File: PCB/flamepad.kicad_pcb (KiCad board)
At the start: 2 copper layers, 77.7 x 96.9 mm, 26 parts, among them J1 Conn_01x04_Pin, SW1 RotaryEncoder_Switch, SW10 SW_Push, SW11 SW_Push, SW12 SW_Push, SW2 SW_Push, SW3 SW_Push, SW4 SW_Push, SW5 SW_Push, SW6 SW_Push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

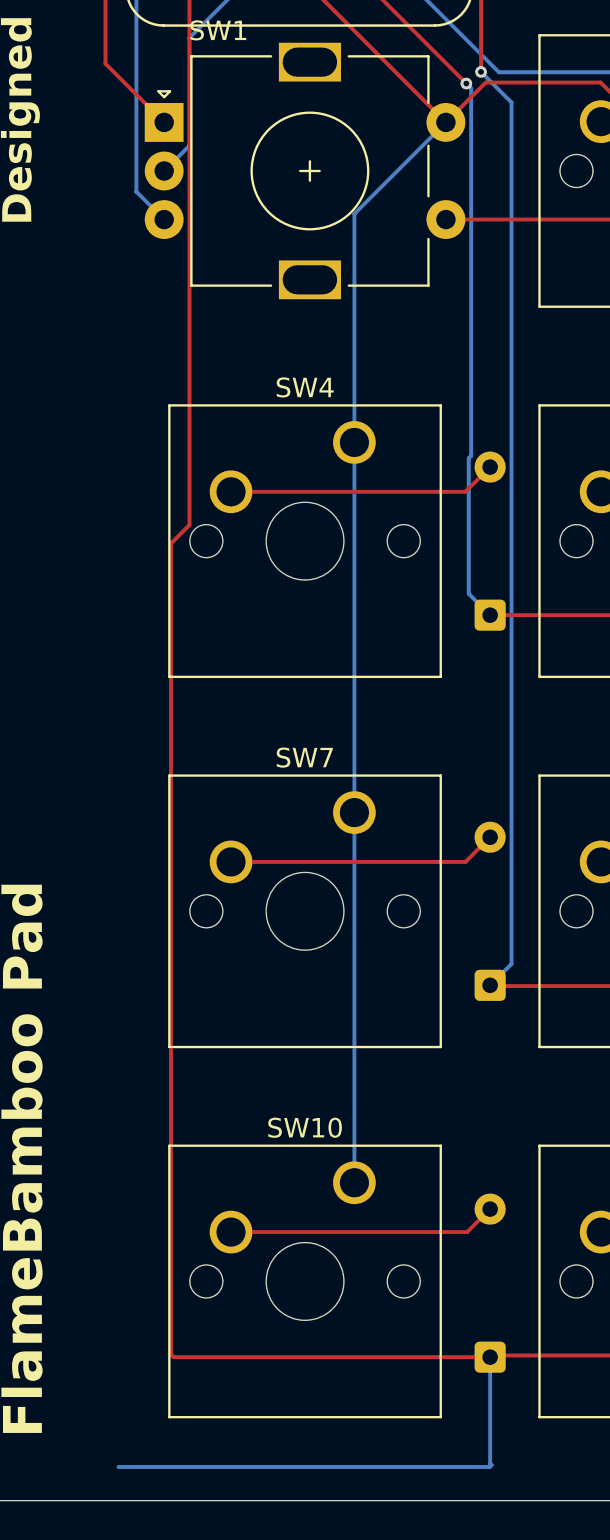
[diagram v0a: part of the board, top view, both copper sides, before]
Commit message: prodfil Gerber update due to mislook mistake in DRC check.
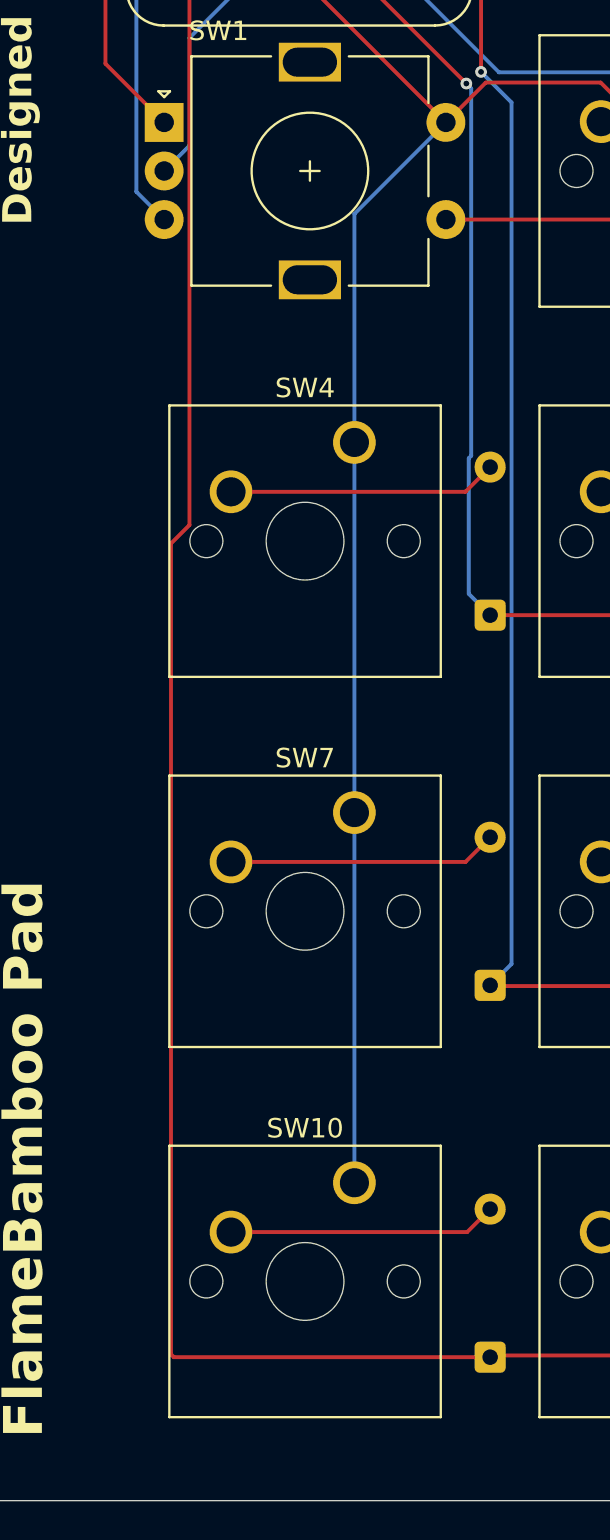
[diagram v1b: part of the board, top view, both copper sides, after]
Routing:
- net Row 3: track 159.5 -> 134.6 mm
- net SW1 A: vias 2 -> 0
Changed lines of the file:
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@@
 			(outputformat 1)
 			(mirror no)
-			(drillshape 1)
+			(drillshape 0)
 			(scaleselection 1)
-			(outputdirectory "")
+			(outputdirectory "../production/")
 		)
 	)
@@
 		(property ki_fp_filters "RotaryEncoder*Switch*")
 		(sheetname "/")
-		(sheetfile "test.kicad_sch")
+		(sheetfile "flamepad.kicad_sch")
 		(attr through_hole)
 		(fp_line
@@
 		)
 		(sheetname "/")
-		(sheetfile "test.kicad_sch")
+		(sheetfile "flamepad.kicad_sch")
 		(attr through_hole)
 		(fp_line
@@
 		)
 		(sheetname "/")
-		(sheetfile "test.kicad_sch")
+		(sheetfile "flamepad.kicad_sch")
 		(attr through_hole)
 		(fp_line
@@
 		(property ki_fp_filters "Connector*:*_1x??_*")
 		(sheetname "/")
-		(sheetfile "test.kicad_sch")
+		(sheetfile "flamepad.kicad_sch")
 		(attr through_hole)
 		(fp_line
@@
 		)
 		(sheetname "/")
-		(sheetfile "test.kicad_sch")
+		(sheetfile "flamepad.kicad_sch")
 		(attr through_hole)
 		(fp_line
@@
 		)
 		(sheetname "/")
-		(sheetfile "test.kicad_sch")
+		(sheetfile "flamepad.kicad_sch")
 		(attr through_hole)
 		(fp_line
@@
 		)
 		(sheetname "/")
-		(sheetfile "test.kicad_sch")
+		(sheetfile "flamepad.kicad_sch")
 		(attr through_hole)
 		(fp_line
@@
 		)
 		(sheetname "/")
-		(sheetfile "test.kicad_sch")
+		(sheetfile "flamepad.kicad_sch")
 		(attr through_hole)
 		(fp_line
@@
 		)
 		(sheetname "/")
-		(sheetfile "test.kicad_sch")
+		(sheetfile "flamepad.kicad_sch")
 		(attr through_hole)
 		(fp_line
@@
 		)
 		(sheetname "/")
-		(sheetfile "test.kicad_sch")
+		(sheetfile "flamepad.kicad_sch")
 		(attr through_hole)
 		(fp_line
@@
 		)
 		(sheetname "/")
-		(sheetfile "test.kicad_sch")
+		(sheetfile "flamepad.kicad_sch")
 		(attr through_hole)
 		(fp_line
@@
 		)
 		(sheetname "/")
-		(sheetfile "test.kicad_sch")
+		(sheetfile "flamepad.kicad_sch")
 		(attr smd)
 		(fp_line
@@
 		)
 		(sheetname "/")
-		(sheetfile "test.kicad_sch")
+		(sheetfile "flamepad.kicad_sch")
 		(attr through_hole)
 		(fp_line
@@
 		)
 		(sheetname "/")
-		(sheetfile "test.kicad_sch")
+		(sheetfile "flamepad.kicad_sch")
 		(attr through_hole)
 		(fp_line
@@
 		(property ki_fp_filters "D*DO?35*")
 		(sheetname "/")
-		(sheetfile "test.kicad_sch")
+		(sheetfile "flamepad.kicad_sch")
 		(attr through_hole)
 		(fp_line
@@
 		(property ki_fp_filters "D*DO?35*")
 		(sheetname "/")
-		(sheetfile "test.kicad_sch")
+		(sheetfile "flamepad.kicad_sch")
 		(attr through_hole)
 		(fp_line
@@
 		(property ki_fp_filters "D*DO?35*")
 		(sheetname "/")
-		(sheetfile "test.kicad_sch")
+		(sheetfile "flamepad.kicad_sch")
 		(attr through_hole)
 		(fp_line
@@
 		(property ki_fp_filters "D*DO?35*")
 		(sheetname "/")
-		(sheetfile "test.kicad_sch")
+		(sheetfile "flamepad.kicad_sch")
 		(attr through_hole)
 		(fp_line
@@
 		(property ki_fp_filters "D*DO?35*")
 		(sheetname "/")
-		(sheetfile "test.kicad_sch")
+		(sheetfile "flamepad.kicad_sch")
 		(attr through_hole)
 		(fp_line
@@
 		(property ki_fp_filters "D*DO?35*")
 		(sheetname "/")
-		(sheetfile "test.kicad_sch")
+		(sheetfile "flamepad.kicad_sch")
 		(attr through_hole)
 		(fp_line
@@
 		(property ki_fp_filters "D*DO?35*")
 		(sheetname "/")
-		(sheetfile "test.kicad_sch")
+		(sheetfile "flamepad.kicad_sch")
 		(attr through_hole)
 		(fp_line
@@
 		(property ki_fp_filters "D*DO?35*")
 		(sheetname "/")
-		(sheetfile "test.kicad_sch")
+		(sheetfile "flamepad.kicad_sch")
 		(attr through_hole)
 		(fp_line
@@
 		(property ki_fp_filters "D*DO?35*")
 		(sheetname "/")
-		(sheetfile "test.kicad_sch")
+		(sheetfile "flamepad.kicad_sch")
 		(attr through_hole)
 		(fp_line
@@
 		(property ki_fp_filters "D*DO?35*")
 		(sheetname "/")
-		(sheetfile "test.kicad_sch")
+		(sheetfile "flamepad.kicad_sch")
 		(attr through_hole)
 		(fp_line
@@
 		(property ki_fp_filters "D*DO?35*")
 		(sheetname "/")
-		(sheetfile "test.kicad_sch")
+		(sheetfile "flamepad.kicad_sch")
 		(attr through_hole)
 		(fp_line
@@
 		(property ki_fp_filters "D*DO?35*")
 		(sheetname "/")
-		(sheetfile "test.kicad_sch")
+		(sheetfile "flamepad.kicad_sch")
 		(attr through_hole)
 		(fp_line
@@
 		(net 20)
 	)
-	(via
-		(at 109.05 79)
-		(size 0.6)
-		(drill 0.3)
-		(layers "F.Cu" "B.Cu")
-		(net 20)
-	)
-	(via
-		(at 109.05 79)
-		(size 0.6)
-		(drill 0.3)
-		(layers "F.Cu" "B.Cu")
-		(net 20)
-	)
 	(segment
 		(start 107.618001 82.568001)
@@
 		(net 22)
 	)
-	(segment
-		(start 106.7 148.2)
-		(end 125.8 148.2)
-		(width 0.2)
-		(layer "B.Cu")
-		(net 22)
-	)
-	(segment
-		(start 125.9 148.1)
-		(end 125.825 148.025)
-		(width 0.2)
-		(layer "B.Cu")
-		(net 22)
-	)
-	(segment
-		(start 125.8 148.2)
-		(end 125.9 148.1)
-		(width 0.2)
-		(layer "B.Cu")
-		(net 22)
-	)
-	(segment
-		(start 125.825 148.025)
-		(end 125.825 142.5475)
-		(width 0.2)
-		(layer "B.Cu")
-		(net 22)
-	)
